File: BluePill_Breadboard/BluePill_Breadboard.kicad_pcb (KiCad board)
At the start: 2 copper layers, 100 x 99.8 mm, 257 parts

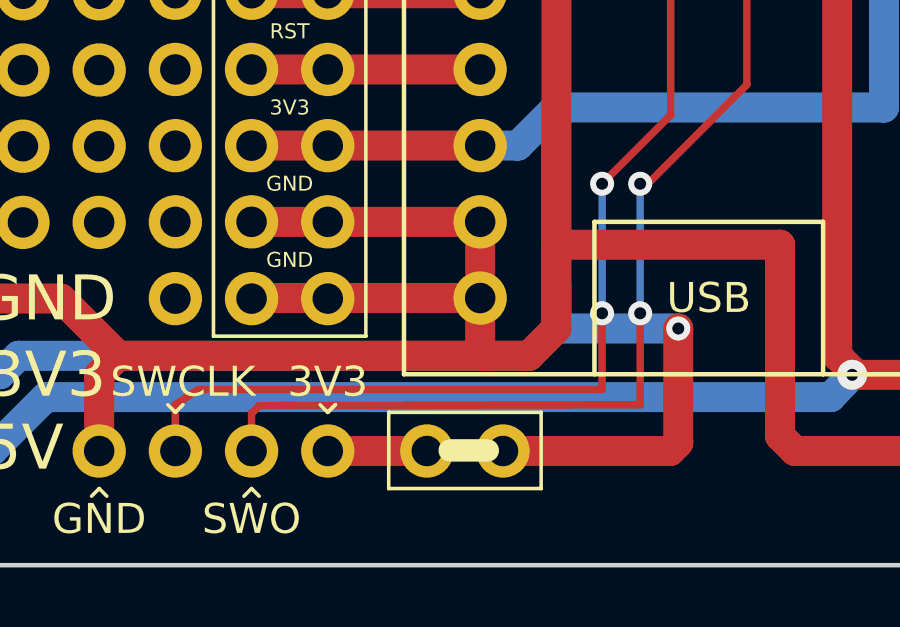
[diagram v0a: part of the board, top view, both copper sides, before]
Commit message: BluePill Board Fix
Fixed 2 Contactpoints were SWO and SWCLK were Connected to 3V3
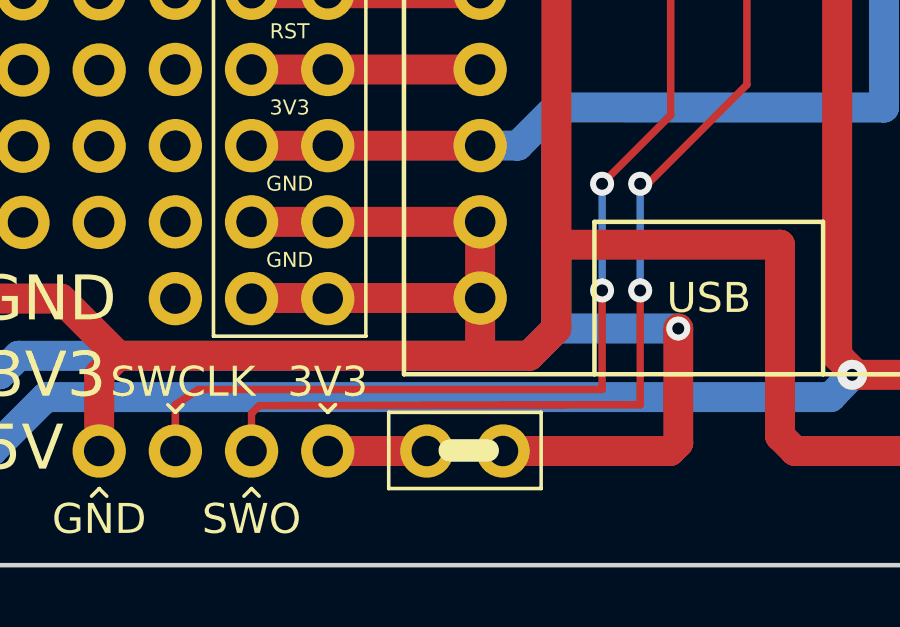
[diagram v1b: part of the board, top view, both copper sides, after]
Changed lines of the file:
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@@
       (drillshape 0)
       (scaleselection 1)
-      (outputdirectory ""))
+      (outputdirectory "Gerber/"))
   )
   (net 0 "")
@@
   (segment (start 143.51 88.665) (end 143.51 89.922235) (width 0.25) (layer F.Cu) (net 0))
   (via (at 139.954 129.286) (size 0.8) (drill 0.4) (layers F.Cu B.Cu) (net 0))
-  (segment (start 138.684 129.286) (end 138.684 133.604) (width 0.25) (layer B.Cu) (net 0))
   (via (at 138.684 129.286) (size 0.8) (drill 0.4) (layers F.Cu B.Cu) (net 0))
-  (via (at 139.954 133.604) (size 0.8) (drill 0.4) (layers F.Cu B.Cu) (net 0))
-  (via (at 138.684 133.604) (size 0.8) (drill 0.4) (layers F.Cu B.Cu) (net 0))
+  (via (at 139.954 132.842) (size 0.8) (drill 0.4) (layers F.Cu B.Cu) (net 0))
+  (via (at 138.684 132.842) (size 0.8) (drill 0.4) (layers F.Cu B.Cu) (net 0))
   (segment (start 121.92 135.655) (end 121.92 138.195) (width 1) (layer F.Cu) (net 0))
   (segment (start 122.555 135.02) (end 121.92 135.655) (width 1) (layer F.Cu) (net 0))
   (segment (start 129.54 138.195) (end 132.842 138.195) (width 1) (layer F.Cu) (net 0))
-  (segment (start 138.684 136.144) (end 138.684 133.604) (width 0.25) (layer F.Cu) (net 0))
   (segment (start 148.082 87.376) (end 149.86 87.376) (width 1) (layer F.Cu) (net 0))
   (segment (start 137.16 89.9255) (end 139.446 87.6395) (width 1) (layer F.Cu) (net 0))
@@
   (segment (start 136.252 135.02) (end 137.16 134.112) (width 1) (layer F.Cu) (net 0))
   (segment (start 137.16 134.112) (end 141.224 134.112) (width 1) (layer B.Cu) (net 0))
-  (segment (start 139.954 129.286) (end 139.954 133.604) (width 0.25) (layer B.Cu) (net 0))
-  (segment (start 139.954 133.604) (end 139.954 136.652) (width 0.25) (layer F.Cu) (net 0))
   (segment (start 141.224 134.112) (end 141.224 134.112) (width 1) (layer B.Cu) (net 0))
   (via (at 141.224 134.112) (size 0.8) (drill 0.4) (layers F.Cu B.Cu) (net 0))
@@
   (segment (start 140.208 129.286) (end 139.954 129.286) (width 0.25) (layer F.Cu) (net 0))
   (segment (start 143.51 125.984) (end 140.208 129.286) (width 0.25) (layer F.Cu) (net 0))
-  (segment (start 125.222 136.144) (end 138.684 136.144) (width 0.25) (layer F.Cu) (net 0))
-  (segment (start 124.46 138.195) (end 124.46 136.652) (width 0.25) (layer F.Cu) (net 0))
-  (segment (start 124.46 136.652) (end 125.222 136.144) (width 0.25) (layer F.Cu) (net 0))
-  (segment (start 127.254 136.683765) (end 139.954 136.652) (width 0.25) (layer F.Cu) (net 0))
-  (segment (start 127 138.195) (end 127 136.937765) (width 0.25) (layer F.Cu) (net 0))
-  (segment (start 127 136.937765) (end 127.254 136.683765) (width 0.25) (layer F.Cu) (net 0))
   (segment (start 147.326235 88.646) (end 148.082 88.646) (width 1) (layer B.Cu) (net 0))
   (segment (start 147.307235 88.665) (end 147.326235 88.646) (width 1) (layer B.Cu) (net 0))
@@
   (segment (start 148.082 126.746) (end 148.082 88.646) (width 1) (layer B.Cu) (net 0))
   (segment (start 148.082 88.646) (end 148.082 84.836) (width 1) (layer B.Cu) (net 0))
+  (segment (start 138.684 129.286) (end 138.684 132.842) (width 0.25) (layer B.Cu) (net 0))
+  (segment (start 139.954 129.286) (end 139.954 132.842) (width 0.25) (layer B.Cu) (net 0))
+  (segment (start 127 136.937765) (end 127 138.195) (width 0.25) (layer F.Cu) (net 0))
+  (segment (start 127.254 136.683765) (end 127 136.937765) (width 0.25) (layer F.Cu) (net 0))
+  (segment (start 139.954 132.842) (end 139.954 136.652) (width 0.25) (layer F.Cu) (net 0))
+  (segment (start 139.954 136.652) (end 127.254 136.683765) (width 0.25) (layer F.Cu) (net 0))
+  (segment (start 125.222 136.144) (end 138.684 136.144) (width 0.25) (layer F.Cu) (net 0))
+  (segment (start 124.46 138.195) (end 124.46 136.652) (width 0.25) (layer F.Cu) (net 0))
+  (segment (start 138.684 136.144) (end 138.684 132.842) (width 0.25) (layer F.Cu) (net 0))
+  (segment (start 124.46 136.652) (end 125.222 136.144) (width 0.25) (layer F.Cu) (net 0))
 )
